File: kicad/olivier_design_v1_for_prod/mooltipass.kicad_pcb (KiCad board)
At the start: 4 copper layers, 65 parts, among them CON2 CON_10118194-0001LF, P1 CONN_8, P2 CONN_6, P3 CONN_10, P4 CONN_8, P5 CONN_1, P6 CONN_1, P7 CONN_1, P8 CONN_1, Q1 MOS_P, Q2 MOS_N, Q3 MOS_P, Q4 MOS_N, U1 CON_SFV30R-2STE1HLF, U2 CON_7312P0225A13LF, U3 IP4234CZ6,125, U4 ATMEGA32U4_QFN, U5 ST662ACD, U6 AT45DB011D-SSH, U7 CON_STACK_9, X1 16MHz

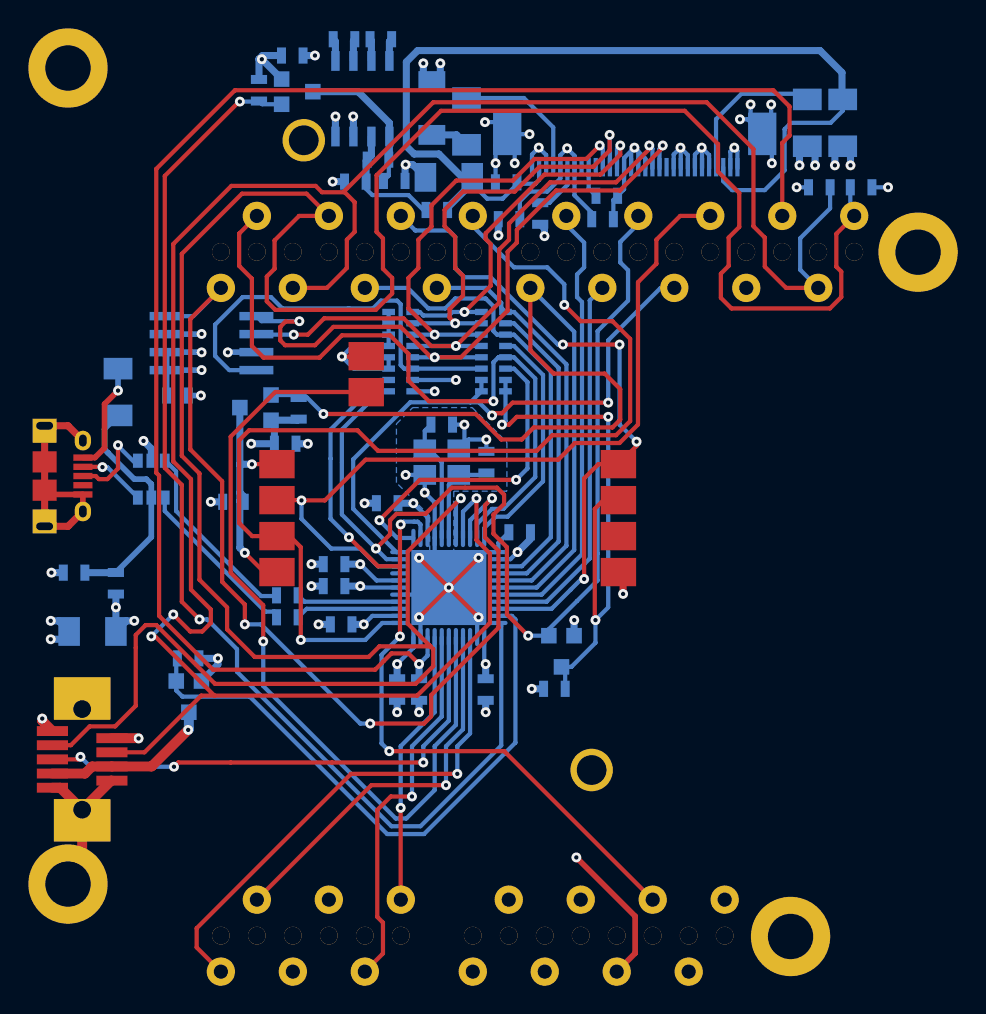
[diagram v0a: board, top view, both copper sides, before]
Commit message: 10k added on gerbers
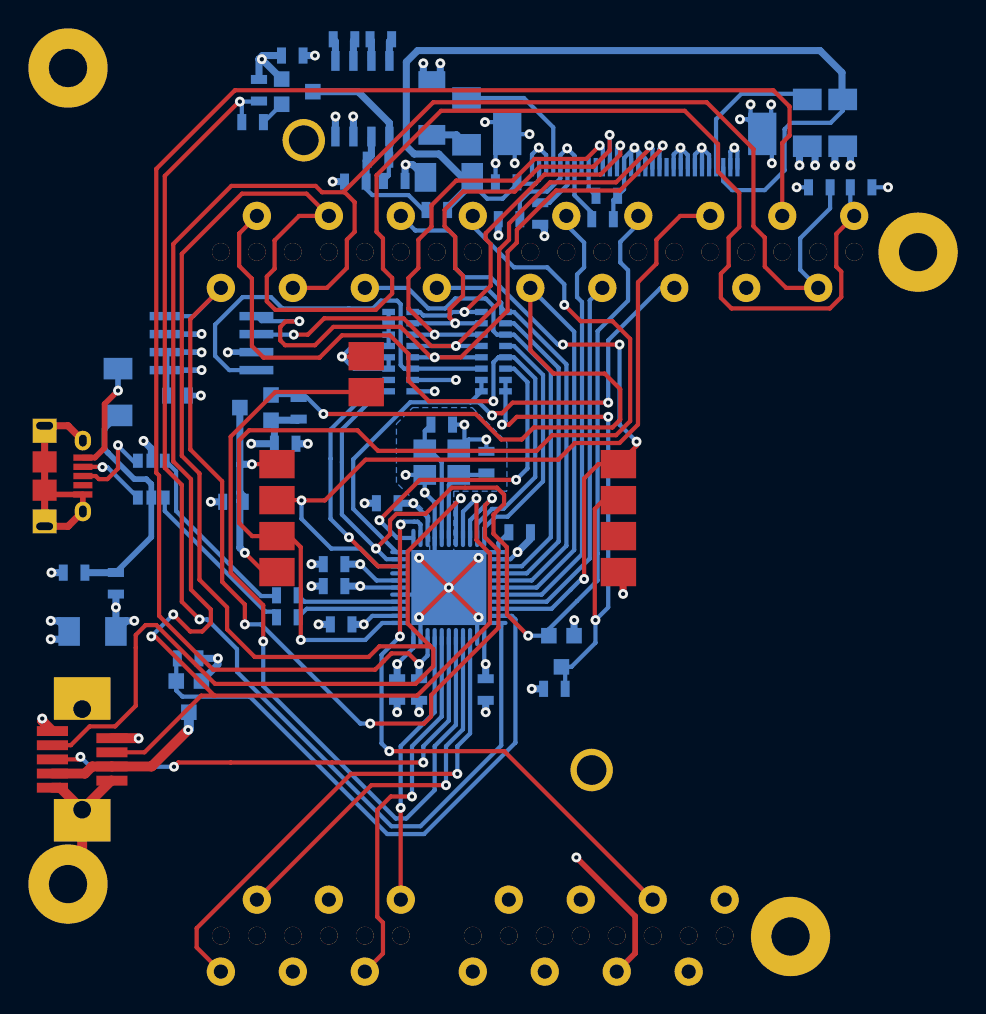
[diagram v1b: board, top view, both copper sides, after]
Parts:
- added R13: 10k, SM0603_Resistor, B.Cu at (123.2, 75.6)
- C1, C3: value 10uF -> 22uF
- P5, P6, P7, P8: footprint HOLE_FIX_M3_SMALL -> HOLE_FIX_M2.5_SMALL
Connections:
- R5 pad 1: /BL_POWER -> N-0000053
- U4 pad 33: /BL_POWER -> N-0000053
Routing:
- net N-0000053: track 0.00 -> 82.0 mm, vias 0 -> 2
- net /BL_POWER: track 82.2 -> 1.81 mm, vias 2 -> 0

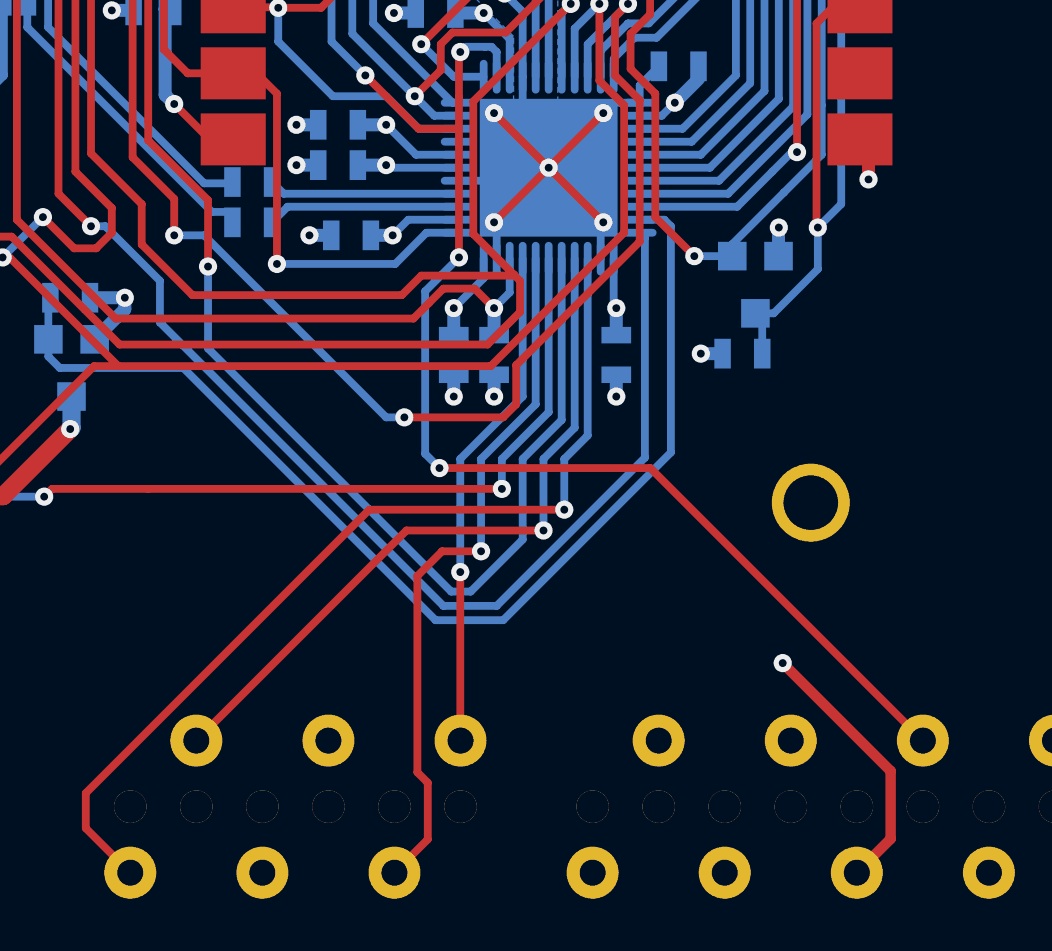
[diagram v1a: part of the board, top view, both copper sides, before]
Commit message: updated gerbers for pinout error
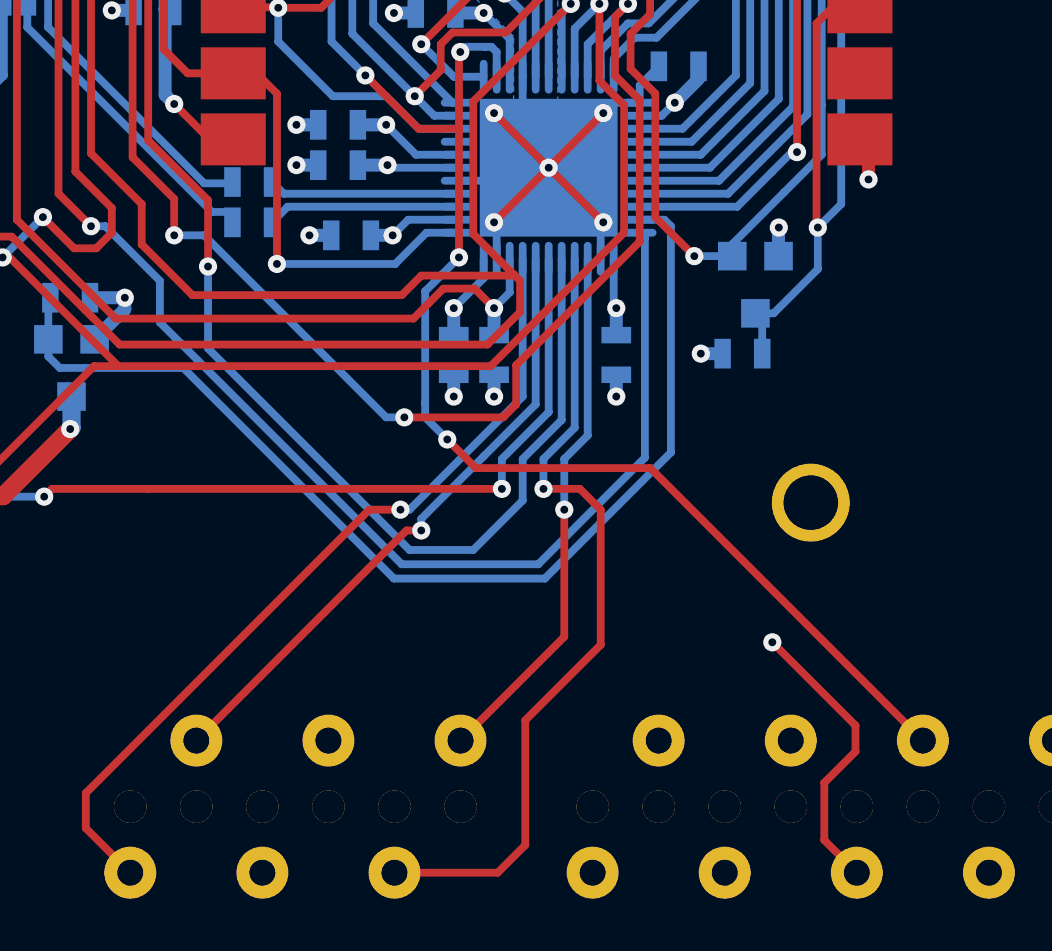
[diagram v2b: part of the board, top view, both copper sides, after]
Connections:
- P2 pad 1: /PF0 -> /PF7
- P2 pad 2: /PF1 -> /PF6
- P2 pad 5: /PF6 -> /PF1
- P2 pad 6: /PF7 -> /PF0
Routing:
- net +3.3V: track 119.5 -> 87.5 mm
- net /PF7: track 36.7 -> 20.6 mm
- net /PF0: track 19.5 -> 32.2 mm
- net /PF6: track 27.6 -> 31.4 mm
- net /PF1: track 27.1 -> 24.3 mm
- net /DETECT_SC: track 58.3 -> 56.1 mm
- net /LED_PWM: track 43.1 -> 41.8 mm
- net N-0000053: track 82.0 -> 80.7 mm
- net /nRESET: track 60.4 -> 59.6 mm
